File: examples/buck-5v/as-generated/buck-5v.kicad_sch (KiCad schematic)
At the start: 11 parts, among them J1 12V IN, J2 5V OUT, U1 LM2596S-5

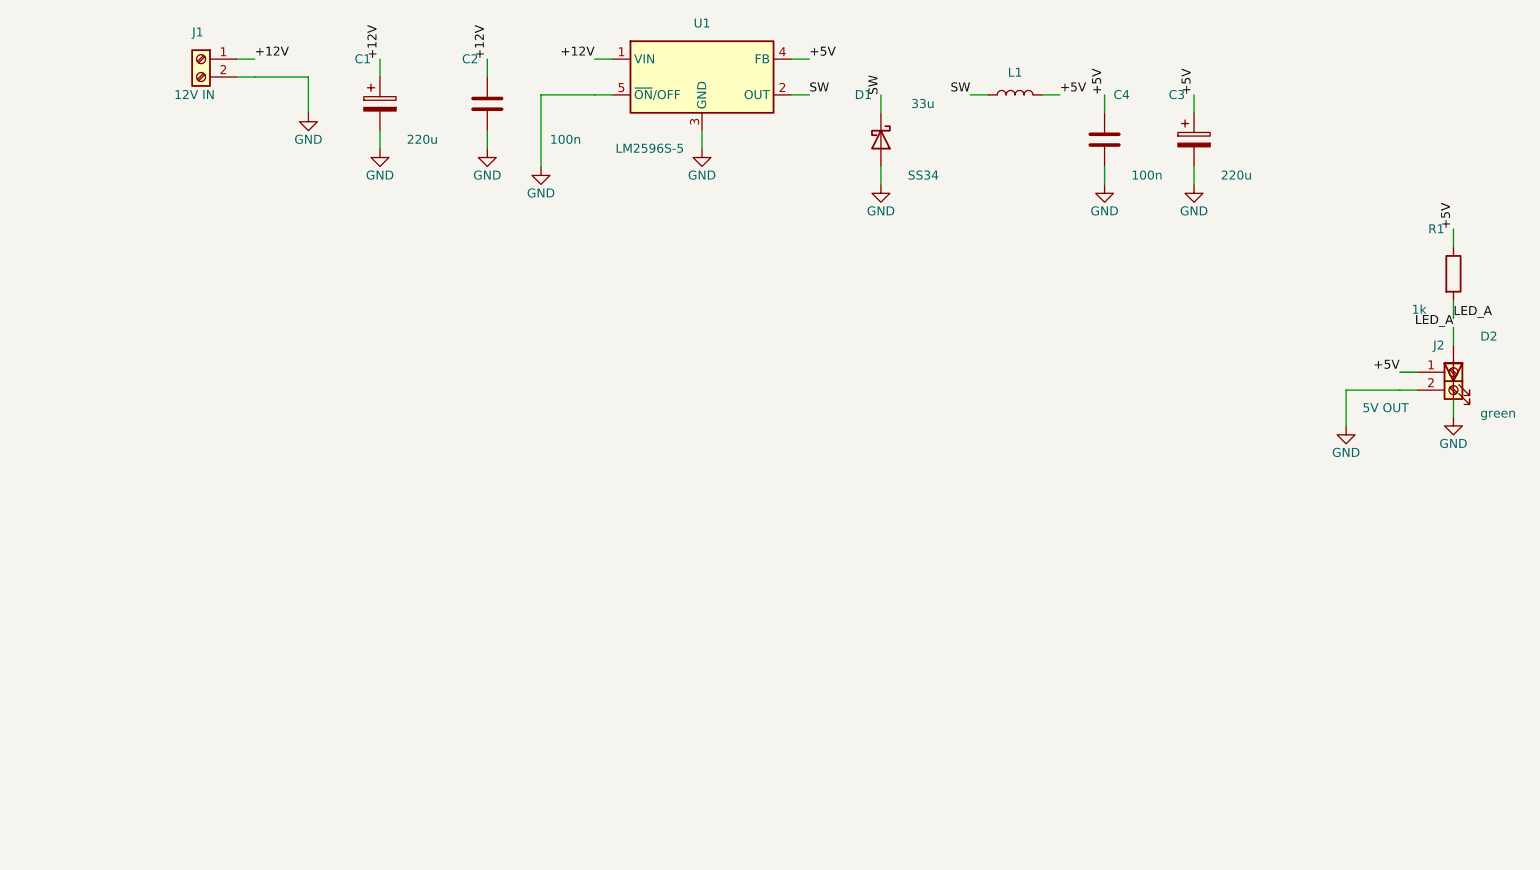
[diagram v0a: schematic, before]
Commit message: Relieve the pads, fillet the joints, and give the board its screw holes
Three of the reviewer's manufacturing points, and they largely fall out
of the one before it - once KiCad fills the plane, the thermal relief it
was already asked for in the file actually appears.

**Thermal relief.** The zones said thermal all along; our own filler
ignored it and flooded every land solid. KiCad's does not, so every
through-hole ground pad now sits in a gap bridged by four spokes and an
iron can bring the joint up without heating a hundred square millimetres
of copper. `layout.solid_pad_connection` reports the setting when a
board turns it off: drilled pads only, because a surface pad reflows in
an oven that is heating the plane anyway and flooding it is often the
better thermal answer.

**Teardrops.** A track entering a land is a step change in width, and a
step change is where copper tears - the connector gets levered on and
off, the drill wanders, and the crack starts at the corner. `_teardrops`
replaces the first stretch of each run with a three-step taper into the
land, checked against its neighbours before it is kept, so a fillet
never eats the clearance a fine-pitch escape needs. It *replaces* rather
than overlays: laying the taper on top of the run drew the same copper
twice, and `route.acute_angle` reported all thirty of them, correctly.
`route.mixed_track_widths` learns what a fillet looks like so a properly
filleted board does not read as one nobody decided the width of.

**Mounting holes.** Four M3 holes near the corners, placed before the
router runs because they are obstacles, and slid along the edges or a
little inboard where a connector body has the corner - the motor board
and the op-amp take three, which is what those floorplans have room for.
Grounded on the motor driver, whose chassis is metal and part of the
shield, plain on the rest: bonding the enclosure to the reference is the
enclosure's decision, not the board's.

Two things that fell out of placing par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
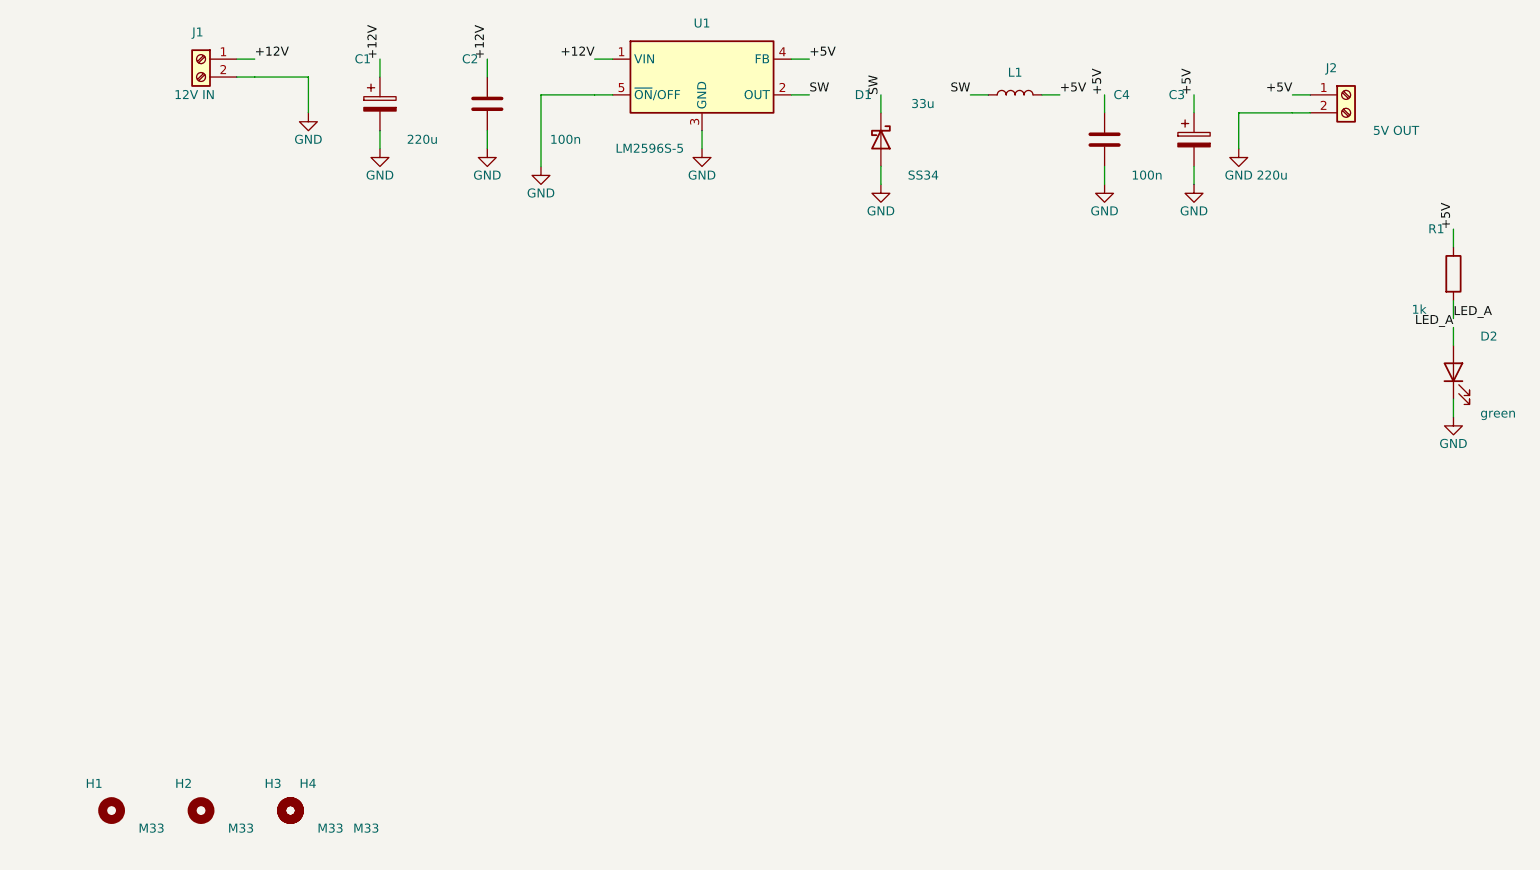
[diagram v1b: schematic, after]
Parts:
- added H1, H2, H3, H4: M33, MountingHole:MountingHole_3.2mm_M3, symbol Mechanical:MountingHole
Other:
- moved on the sheet: J2
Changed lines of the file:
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@@
     (exclude_from_sim no) (in_bom yes) (on_board yes) (dnp no)
     (property "Reference" "C3" (at 178.11 68.39 0) (effects (font (size 1.27 1.27)) (justify right)))
-    (property "Value" "220u" (at 183.19 79.82 0) (effects (font (size 1.27 1.27)) (justify left)))
+    (property "Value" "220u" (at 188.27 79.82 0) (effects (font (size 1.27 1.27)) (justify left)))
     (property "Footprint" "Capacitor_SMD:CP_Elec_8x10.5" (at 179.38 74.74 0) (effects (font (size 1.27 1.27)) hide))
     (property "Datasheet" "https://industrial.panasonic.com/cdbs/www-data/pdf/RDF0000/ABA0000C1053.pdf" (at 179.38 74.74 0) (effects (font (size 1.27 1.27)) hide))
@@
     (instances (project "buck-5v" (path "/ec98644d-848c-5056-a4cb-c829189be5c3" (reference "D2") (unit 1))))
   )
-  (wire (pts (xy 211.13 107.76) (xy 208.59 107.76)) (stroke (width 0) (type default)))
-  (label "+5V" (at 208.59 107.76 0) (effects (font (size 1.27 1.27)) (justify right bottom)))
-  (wire (pts (xy 211.13 110.3) (xy 208.59 110.3)) (stroke (width 0) (type default)))
-  (symbol (lib_id "Connector:Screw_Terminal_01x02") (at 216.21 107.76 0.0) (unit 1)
+  (wire (pts (xy 195.89 68.39) (xy 193.35 68.39)) (stroke (width 0) (type default)))
+  (label "+5V" (at 193.35 68.39 0) (effects (font (size 1.27 1.27)) (justify right bottom)))
+  (wire (pts (xy 195.89 70.93) (xy 193.35 70.93)) (stroke (width 0) (type default)))
+  (symbol (lib_id "Connector:Screw_Terminal_01x02") (at 200.97 68.39 0.0) (unit 1)
     (exclude_from_sim no) (in_bom yes) (on_board yes) (dnp no)
-    (property "Reference" "J2" (at 214.94 103.95 0) (effects (font (size 1.27 1.27)) (justify right)))
-    (property "Value" "5V OUT" (at 209.86 112.84 0) (effects (font (size 1.27 1.27)) (justify right)))
-    (property "Footprint" "TerminalBlock_Phoenix:TerminalBlock_Phoenix_MKDS-1,5-2_1x02_P5.00mm_Horizontal" (at 216.21 107.76 0) (effects (font (size 1.27 1.27)) hide))
-    (property "Datasheet" "https://www.phoenixcontact.com/product/1729128" (at 216.21 107.76 0) (effects (font (size 1.27 1.27)) hide))
+    (property "Reference" "J2" (at 199.7 64.58 0) (effects (font (size 1.27 1.27)) (justify right)))
+    (property "Value" "5V OUT" (at 204.78 73.47 0) (effects (font (size 1.27 1.27)) (justify left)))
+    (property "Footprint" "TerminalBlock_Phoenix:TerminalBlock_Phoenix_MKDS-1,5-2_1x02_P5.00mm_Horizontal" (at 200.97 68.39 0) (effects (font (size 1.27 1.27)) hide))
+    (property "Datasheet" "https://www.phoenixcontact.com/product/1729128" (at 200.97 68.39 0) (effects (font (size 1.27 1.27)) hide))
     (pin "1" (uuid "5a0aab3c-0494-5596-922b-fe757aeb0a1c-p1"))
     (pin "2" (uuid "5a0aab3c-0494-5596-922b-fe757aeb0a1c-p2"))
     (instances (project "buck-5v" (path "/ec98644d-848c-5056-a4cb-c829189be5c3" (reference "J2") (unit 1))))
+  )
+  (symbol (lib_id "Mechanical:MountingHole") (at 25.71 169.99 0.0) (unit 1)
+    (exclude_from_sim no) (in_bom yes) (on_board yes) (dnp no)
+    (property "Reference" "H1" (at 24.44 166.18 0) (effects (font (size 1.27 1.27)) (justify right)))
+    (property "Value" "M33" (at 29.52 172.53 0) (effects (font (size 1.27 1.27)) (justify left)))
+    (property "Footprint" "MountingHole:MountingHole_3.2mm_M3" (at 25.71 169.99 0) (effects (font (size 1.27 1.27)) hide))
+    (property "Datasheet" "~" (at 25.71 169.99 0) (effects (font (size 1.27 1.27)) hide))
+    (instances (project "buck-5v" (path "/ec98644d-848c-5056-a4cb-c829189be5c3" (reference "H1") (unit 1))))
+  )
+  (symbol (lib_id "Mechanical:MountingHole") (at 38.41 169.99 0.0) (unit 1)
+    (exclude_from_sim no) (in_bom yes) (on_board yes) (dnp no)
+    (property "Reference" "H2" (at 37.14 166.18 0) (effects (font (size 1.27 1.27)) (justify right)))
+    (property "Value" "M33" (at 42.22 172.53 0) (effects (font (size 1.27 1.27)) (justify left)))
+    (property "Footprint" "MountingHole:MountingHole_3.2mm_M3" (at 38.41 169.99 0) (effects (font (size 1.27 1.27)) hide))
+    (property "Datasheet" "~" (at 38.41 169.99 0) (effects (font (size 1.27 1.27)) hide))
+    (instances (project "buck-5v" (path "/ec98644d-848c-5056-a4cb-c829189be5c3" (reference "H2") (unit 1))))
+  )
+  (symbol (lib_id "Mechanical:MountingHole") (at 51.11 169.99 0.0) (unit 1)
+    (exclude_from_sim no) (in_bom yes) (on_board yes) (dnp no)
+    (property "Reference" "H3" (at 49.84 166.18 0) (effects (font (size 1.27 1.27)) (justify right)))
+    (property "Value" "M33" (at 54.92 172.53 0) (effects (font (size 1.27 1.27)) (justify left)))
+    (property "Footprint" "MountingHole:MountingHole_3.2mm_M3" (at 51.11 169.99 0) (effects (font (size 1.27 1.27)) hide))
+    (property "Datasheet" "~" (at 51.11 169.99 0) (effects (font (size 1.27 1.27)) hide))
+    (instances (project "buck-5v" (path "/ec98644d-848c-5056-a4cb-c829189be5c3" (reference "H3") (unit 1))))
+  )
+  (symbol (lib_id "Mechanical:MountingHole") (at 51.11 169.99 0.0) (unit 1)
+    (exclude_from_sim no) (in_bom yes) (on_board yes) (dnp no)
+    (property "Reference" "H4" (at 52.38 166.18 0) (effects (font (size 1.27 1.27)) (justify left)))
+    (property "Value" "M33" (at 60.0 172.53 0) (effects (font (size 1.27 1.27)) (justify left)))
+    (property "Footprint" "MountingHole:MountingHole_3.2mm_M3" (at 51.11 169.99 0) (effects (font (size 1.27 1.27)) hide))
+    (property "Datasheet" "~" (at 51.11 169.99 0) (effects (font (size 1.27 1.27)) hide))
+    (instances (project "buck-5v" (path "/ec98644d-848c-5056-a4cb-c829189be5c3" (reference "H4") (unit 1))))
   )
   (wire (pts (xy 46.03 65.85) (xy 53.65 65.85)) (stroke (width 0) (type default)))
@@
   (wire (pts (xy 94.29 68.39) (xy 86.67 68.39)) (stroke (width 0) (type default)))
   (wire (pts (xy 86.67 68.39) (xy 86.67 78.55)) (stroke (width 0) (type default)))
-  (wire (pts (xy 208.59 110.3) (xy 200.97 110.3)) (stroke (width 0) (type default)))
-  (wire (pts (xy 200.97 110.3) (xy 200.97 115.38)) (stroke (width 0) (type default)))
+  (wire (pts (xy 193.35 70.93) (xy 185.73 70.93)) (stroke (width 0) (type default)))
+  (wire (pts (xy 185.73 70.93) (xy 185.73 76.01)) (stroke (width 0) (type default)))
   (symbol (lib_id "power:GND") (at 53.65 70.93 0) (unit 1)
     (exclude_from_sim no) (in_bom no) (on_board yes) (dnp no)
@@
     (instances (project "buck-5v" (path "/ec98644d-848c-5056-a4cb-c829189be5c3" (reference "#PWR09") (unit 1))))
   )
-  (symbol (lib_id "power:GND") (at 200.97 115.38 0) (unit 1)
+  (symbol (lib_id "power:GND") (at 185.73 76.01 0) (unit 1)
     (exclude_from_sim no) (in_bom no) (on_board yes) (dnp no)
-    (property "Reference" "#PWR10" (at 200.97 115.38 0) (effects (font (size 1.27 1.27)) hide))
-    (property "Value" "GND" (at 200.97 119.19 0) (effects (font (size 1.27 1.27))))
-    (property "Footprint" "" (at 200.97 115.38 0) (effects (font (size 1.27 1.27)) hide))
-    (property "Datasheet" "" (at 200.97 115.38 0) (effects (font (size 1.27 1.27)) hide))
+    (property "Reference" "#PWR10" (at 185.73 76.01 0) (effects (font (size 1.27 1.27)) hide))
+    (property "Value" "GND" (at 185.73 79.82 0) (effects (font (size 1.27 1.27))))
+    (property "Footprint" "" (at 185.73 76.01 0) (effects (font (size 1.27 1.27)) hide))
+    (property "Datasheet" "" (at 185.73 76.01 0) (effects (font (size 1.27 1.27)) hide))
     (pin "1" (uuid "a43010a0-3ea2-5100-9bd2-2c0a54c03dac-p"))
     (instances (project "buck-5v" (path "/ec98644d-848c-5056-a4cb-c829189be5c3" (reference "#PWR10") (unit 1))))

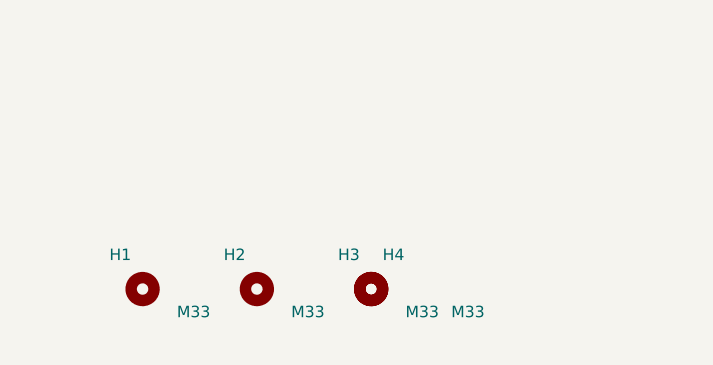
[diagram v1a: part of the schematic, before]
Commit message: Give the assembly machine something to aim at
Fiducials: three copper dots in bare mask windows, near three different
corners so a pick-and-place gets rotation as well as offset. It aligns
to the board, not to the drawing - without them it has only the routed
outline, cut to a tolerance ten times looser than the placement a 0.5 mm
pitch part is asking for. `fab.no_fiducials` reports a fine-pitch board
that has none, as context rather than as a fault: plenty of boards are
built one at a time with tweezers.

They share the corner search with the mounting holes, which is where
this found a real bug: `_courtyard_box` read lines and rectangles only,
and a mounting hole draws its courtyard as one circle - so every hole
measured as taking up no room at all, and the first three fiducials
landed on top of three screw holes. Circles and arcs count now.

Co-Authored-By: Claude Fable 5 <noreply@anthropic.com>
Claude-Session: https://claude.ai/code/session_01DUj7Ltu92tWg159mCSacwY
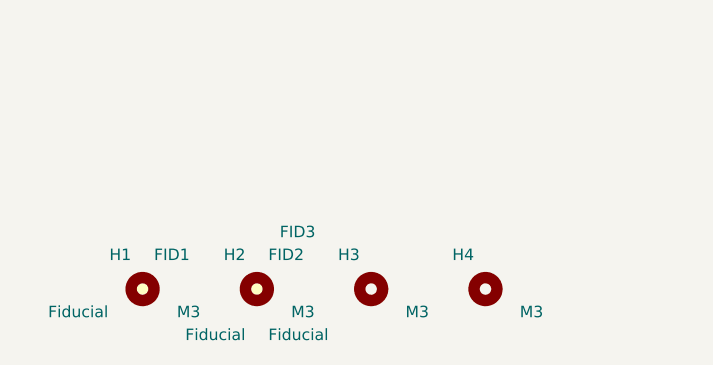
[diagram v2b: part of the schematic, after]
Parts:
- added FID1, FID2, FID3: Fiducial, Fiducial:Fiducial_1mm_Mask2mm, symbol Mechanical:Fiducial
- H1, H2, H3, H4: value M33 -> M3
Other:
- moved on the sheet: H4
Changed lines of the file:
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@@
     (exclude_from_sim no) (in_bom yes) (on_board yes) (dnp no)
     (property "Reference" "H1" (at 24.44 166.18 0) (effects (font (size 1.27 1.27)) (justify right)))
-    (property "Value" "M33" (at 29.52 172.53 0) (effects (font (size 1.27 1.27)) (justify left)))
+    (property "Value" "M3" (at 29.52 172.53 0) (effects (font (size 1.27 1.27)) (justify left)))
     (property "Footprint" "MountingHole:MountingHole_3.2mm_M3" (at 25.71 169.99 0) (effects (font (size 1.27 1.27)) hide))
     (property "Datasheet" "~" (at 25.71 169.99 0) (effects (font (size 1.27 1.27)) hide))
@@
     (exclude_from_sim no) (in_bom yes) (on_board yes) (dnp no)
     (property "Reference" "H2" (at 37.14 166.18 0) (effects (font (size 1.27 1.27)) (justify right)))
-    (property "Value" "M33" (at 42.22 172.53 0) (effects (font (size 1.27 1.27)) (justify left)))
+    (property "Value" "M3" (at 42.22 172.53 0) (effects (font (size 1.27 1.27)) (justify left)))
     (property "Footprint" "MountingHole:MountingHole_3.2mm_M3" (at 38.41 169.99 0) (effects (font (size 1.27 1.27)) hide))
     (property "Datasheet" "~" (at 38.41 169.99 0) (effects (font (size 1.27 1.27)) hide))
@@
     (exclude_from_sim no) (in_bom yes) (on_board yes) (dnp no)
     (property "Reference" "H3" (at 49.84 166.18 0) (effects (font (size 1.27 1.27)) (justify right)))
-    (property "Value" "M33" (at 54.92 172.53 0) (effects (font (size 1.27 1.27)) (justify left)))
+    (property "Value" "M3" (at 54.92 172.53 0) (effects (font (size 1.27 1.27)) (justify left)))
     (property "Footprint" "MountingHole:MountingHole_3.2mm_M3" (at 51.11 169.99 0) (effects (font (size 1.27 1.27)) hide))
     (property "Datasheet" "~" (at 51.11 169.99 0) (effects (font (size 1.27 1.27)) hide))
     (instances (project "buck-5v" (path "/ec98644d-848c-5056-a4cb-c829189be5c3" (reference "H3") (unit 1))))
   )
-  (symbol (lib_id "Mechanical:MountingHole") (at 51.11 169.99 0.0) (unit 1)
+  (symbol (lib_id "Mechanical:MountingHole") (at 63.81 169.99 0.0) (unit 1)
     (exclude_from_sim no) (in_bom yes) (on_board yes) (dnp no)
-    (property "Reference" "H4" (at 52.38 166.18 0) (effects (font (size 1.27 1.27)) (justify left)))
-    (property "Value" "M33" (at 60.0 172.53 0) (effects (font (size 1.27 1.27)) (justify left)))
-    (property "Footprint" "MountingHole:MountingHole_3.2mm_M3" (at 51.11 169.99 0) (effects (font (size 1.27 1.27)) hide))
-    (property "Datasheet" "~" (at 51.11 169.99 0) (effects (font (size 1.27 1.27)) hide))
+    (property "Reference" "H4" (at 62.54 166.18 0) (effects (font (size 1.27 1.27)) (justify right)))
+    (property "Value" "M3" (at 67.62 172.53 0) (effects (font (size 1.27 1.27)) (justify left)))
+    (property "Footprint" "MountingHole:MountingHole_3.2mm_M3" (at 63.81 169.99 0) (effects (font (size 1.27 1.27)) hide))
+    (property "Datasheet" "~" (at 63.81 169.99 0) (effects (font (size 1.27 1.27)) hide))
     (instances (project "buck-5v" (path "/ec98644d-848c-5056-a4cb-c829189be5c3" (reference "H4") (unit 1))))
   )
+  (symbol (lib_id "Mechanical:Fiducial") (at 25.71 169.99 0.0) (unit 1)
+    (exclude_from_sim no) (in_bom yes) (on_board yes) (dnp no)
+    (property "Reference" "FID1" (at 26.98 166.18 0) (effects (font (size 1.27 1.27)) (justify left)))
+    (property "Value" "Fiducial" (at 21.9 172.53 0) (effects (font (size 1.27 1.27)) (justify right)))
+    (property "Footprint" "Fiducial:Fiducial_1mm_Mask2mm" (at 25.71 169.99 0) (effects (font (size 1.27 1.27)) hide))
+    (property "Datasheet" "~" (at 25.71 169.99 0) (effects (font (size 1.27 1.27)) hide))
+    (instances (project "buck-5v" (path "/ec98644d-848c-5056-a4cb-c829189be5c3" (reference "FID1") (unit 1))))
+  )
+  (symbol (lib_id "Mechanical:Fiducial") (at 38.41 169.99 0.0) (unit 1)
+    (exclude_from_sim no) (in_bom yes) (on_board yes) (dnp no)
+    (property "Reference" "FID2" (at 39.68 166.18 0) (effects (font (size 1.27 1.27)) (justify left)))
+    (property "Value" "Fiducial" (at 39.68 175.07 0) (effects (font (size 1.27 1.27)) (justify left)))
+    (property "Footprint" "Fiducial:Fiducial_1mm_Mask2mm" (at 38.41 169.99 0) (effects (font (size 1.27 1.27)) hide))
+    (property "Datasheet" "~" (at 38.41 169.99 0) (effects (font (size 1.27 1.27)) hide))
+    (instances (project "buck-5v" (path "/ec98644d-848c-5056-a4cb-c829189be5c3" (reference "FID2") (unit 1))))
+  )
+  (symbol (lib_id "Mechanical:Fiducial") (at 38.41 169.99 0.0) (unit 1)
+    (exclude_from_sim no) (in_bom yes) (on_board yes) (dnp no)
+    (property "Reference" "FID3" (at 40.95 163.64 0) (effects (font (size 1.27 1.27)) (justify left)))
+    (property "Value" "Fiducial" (at 37.14 175.07 0) (effects (font (size 1.27 1.27)) (justify right)))
+    (property "Footprint" "Fiducial:Fiducial_1mm_Mask2mm" (at 38.41 169.99 0) (effects (font (size 1.27 1.27)) hide))
+    (property "Datasheet" "~" (at 38.41 169.99 0) (effects (font (size 1.27 1.27)) hide))
+    (instances (project "buck-5v" (path "/ec98644d-848c-5056-a4cb-c829189be5c3" (reference "FID3") (unit 1))))
+  )
   (wire (pts (xy 46.03 65.85) (xy 53.65 65.85)) (stroke (width 0) (type default)))
